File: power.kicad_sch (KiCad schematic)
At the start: 50 parts, among them J4 Conn_01x02, Q1 Q_NMOS, Q2 Q_NMOS, U2 LDL212PVR, U3 LDL212PVR, U5 LDL212PVR, U6 LDL212PVR, U8 TPS62933O, U9 LM74502

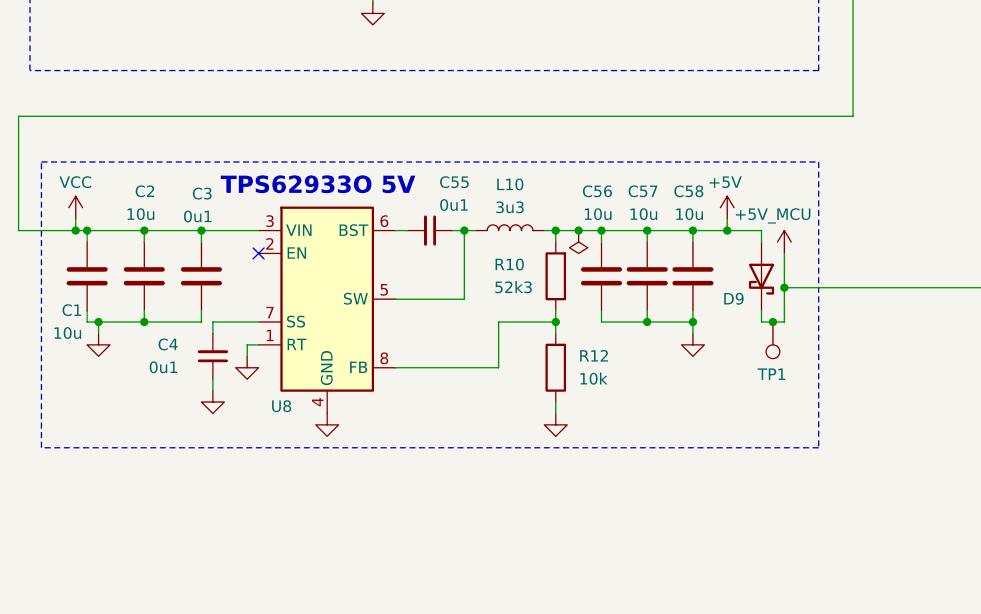
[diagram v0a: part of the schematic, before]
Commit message: schem: add buck converter PG led
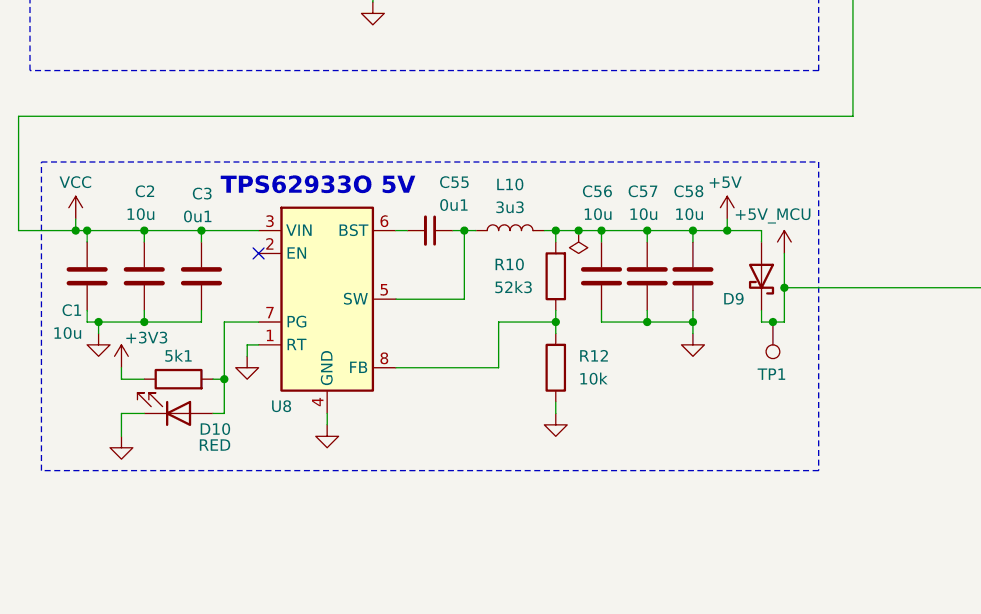
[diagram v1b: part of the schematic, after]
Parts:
- removed C4: 0u1, Capacitor_SMD:C_0402_1005Metric, symbol Device:C_Small
- added D10: RED, LED_SMD:LED_0603_1608Metric, symbol Device:LED
- added R13: 5k1, Resistor_SMD:R_0402_1005Metric, symbol Device:R
- U8: symbol Regulator_Switching:TPS62933 -> Regulator_Switching:TPS62933O
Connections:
- net +3V3: now also R13.1
- net GND: now also D10.1 (K)
- net at U8.7 (PG): now also D10.2 (A), R13.2

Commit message: schem: change red led to lower vf
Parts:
- D10: footprint LED_SMD:LED_0603_1608Metric -> LED_SMD:LED_0805_2012Metric; JLCPCB Part # C2286 -> NCD0805R1; Manufacturer Hubei KENTO Elec -> Foshan NationStar Optoelectronics; Manufacturer Part Number KT-0603R -> NCD0805R1
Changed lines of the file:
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@@
 			)
 		)
-		(property "Footprint" "LED_SMD:LED_0603_1608Metric"
+		(property "Footprint" "LED_SMD:LED_0805_2012Metric"
 			(at 69.85 130.81 0)
 			(hide yes)
@@
 			)
 		)
-		(property "JLCPCB Part #" "C2286"
+		(property "JLCPCB Part #" "NCD0805R1"
 			(at 69.85 130.81 90)
 			(hide yes)
@@
 			)
 		)
-		(property "Manufacturer" "Hubei KENTO Elec "
+		(property "Manufacturer" "Foshan NationStar Optoelectronics"
 			(at 69.85 130.81 90)
 			(hide yes)
@@
 			)
 		)
-		(property "Manufacturer Part Number" "KT-0603R"
+		(property "Manufacturer Part Number" "NCD0805R1"
 			(at 69.85 130.81 90)
 			(hide yes)

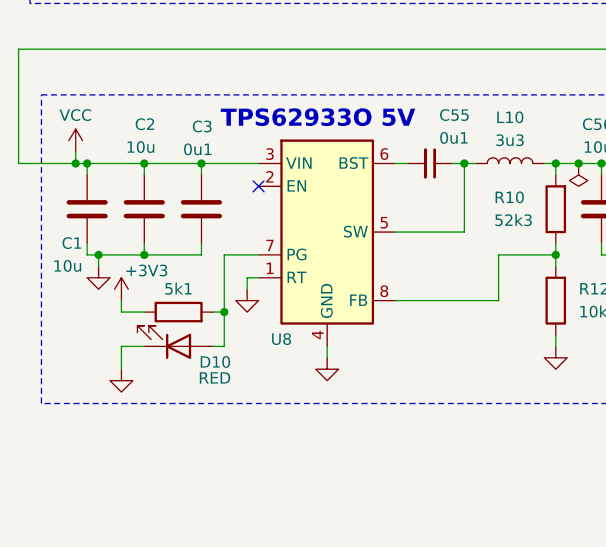
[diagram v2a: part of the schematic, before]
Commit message: schem: add PG gpio to buck converter
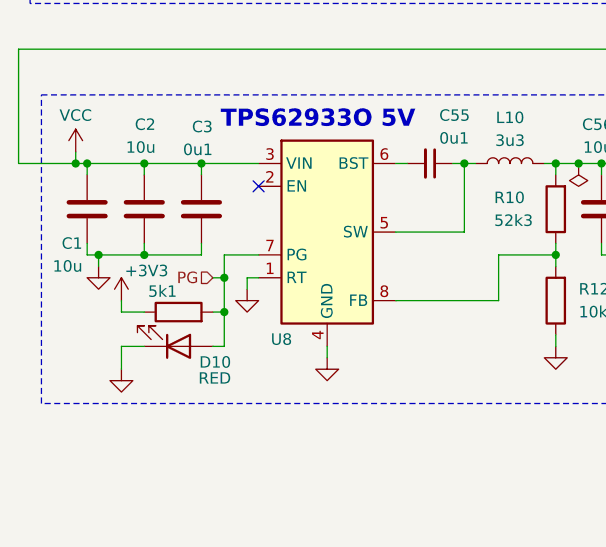
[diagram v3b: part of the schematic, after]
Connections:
- net PG: now reaches D10.2 (A), R13.2, U8.7 (PG)
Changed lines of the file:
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@@
 	)
 	(junction
+		(at 74.93 123.19)
+		(diameter 0)
+		(color 0 0 0 0)
+	)
+	(junction
 		(at 182.88 68.58)
 		(diameter 0)
@@
 	(wire
 		(pts
+			(xy 74.93 123.19) (xy 74.93 127)
+		)
+		(stroke
+			(width 0)
+			(type default)
+		)
+	)
+	(wire
+		(pts
 			(xy 205.74 102.87) (xy 205.74 100.33)
 		)
@@
 	(wire
 		(pts
-			(xy 74.93 120.65) (xy 74.93 127)
+			(xy 74.93 120.65) (xy 74.93 123.19)
 		)
 		(stroke
@@
 	(wire
 		(pts
-			(xy 78.74 120.65) (xy 74.93 120.65)
+			(xy 74.93 120.65) (xy 78.74 120.65)
 		)
 		(stroke
@@
 	(wire
 		(pts
+			(xy 73.66 123.19) (xy 74.93 123.19)
+		)
+		(stroke
+			(width 0)
+			(type default)
+		)
+	)
+	(wire
+		(pts
 			(xy 240.03 35.56) (xy 240.03 36.83)
 		)
@@
 		)
 	)
+	(hierarchical_label "PG"
+		(shape input)
+		(at 73.66 123.19 180)
+		(effects
+			(font
+				(size 1.27 1.27)
+			)
+			(justify right)
+		)
+	)
 	(symbol
 		(lib_id "power:+5V")
@@
 		)
 		(property "Value" "5k1"
-			(at 69.85 124.46 90)
+			(at 68.072 124.714 90)
 			(show_name no)
 			(do_not_autoplace no)

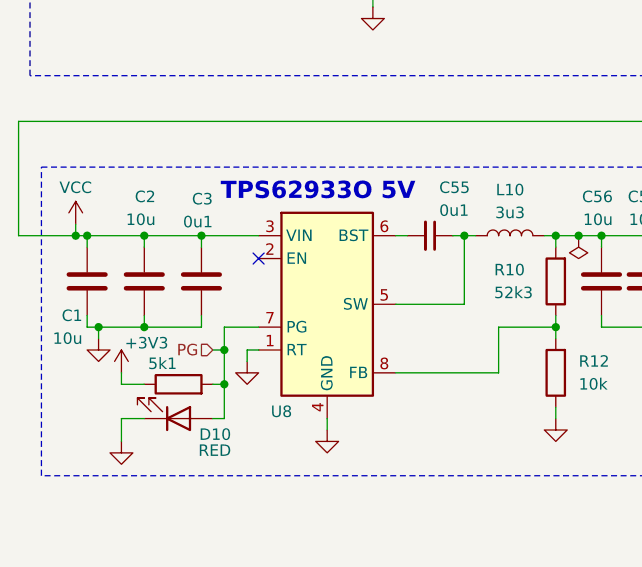
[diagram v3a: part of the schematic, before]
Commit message: schem: add buck converter disable jumper
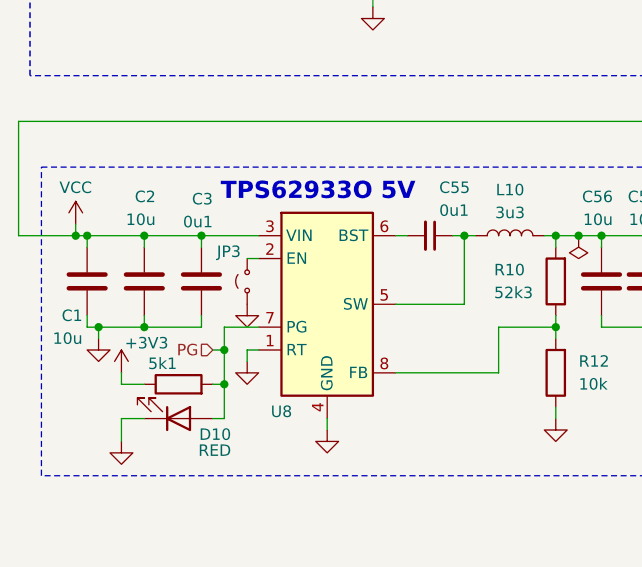
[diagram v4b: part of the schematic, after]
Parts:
- added JP3: Jumper_2_Small_Open, Connector_PinHeader_2.54mm:PinHeader_1x02_P2.54mm_Vertical, symbol Jumper:Jumper_2_Small_Open
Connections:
- net GND: now also JP3.1 (A)
- net at U8.2 (EN): now also JP3.2 (B)
- no-connect marks 1 -> 0
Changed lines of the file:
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@@
 		(color 0 0 0 0)
 	)
-	(no_connect
-		(at 78.74 113.03)
-	)
 	(wire
 		(pts
@@
 	(wire
 		(pts
+			(xy 77.47 113.03) (xy 78.74 113.03)
+		)
+		(stroke
+			(width 0)
+			(type default)
+		)
+	)
+	(wire
+		(pts
 			(xy 78.74 123.19) (xy 77.47 123.19)
 		)
@@
 	)
 	(symbol
+		(lib_id "Jumper:Jumper_2_Small_Open")
+		(at 77.47 115.57 90)
+		(unit 1)
+		(body_style 1)
+		(exclude_from_sim no)
+		(in_bom no)
+		(on_board yes)
+		(in_pos_files yes)
+		(dnp no)
+		(property "Reference" "JP3"
+			(at 75.438 112.268 90)
+			(show_name no)
+			(do_not_autoplace no)
+			(effects
+				(font
+					(size 1.27 1.27)
+				)
+			)
+		)
+		(property "Value" "Jumper_2_Small_Open"
+			(at 78.74 116.8399 90)
+			(hide yes)
+			(show_name no)
+			(do_not_autoplace no)
+			(effects
+				(font
+					(size 1.27 1.27)
+				)
+				(justify right)
+			)
+		)
+		(property "Footprint" "Connector_PinHeader_2.54mm:PinHeader_1x02_P2.54mm_Vertical"
+			(at 77.47 115.57 0)
+			(hide yes)
+			(show_name no)
+			(do_not_autoplace no)
+			(effects
+				(font
+					(size 1.27 1.27)
+				)
+			)
+		)
+		(property "Datasheet" ""
+			(at 77.47 115.57 0)
+			(hide yes)
+			(show_name no)
+			(do_not_autoplace no)
+			(effects
+				(font
+					(size 1.27 1.27)
+				)
+			)
+		)
+		(property "Description" "Jumper, 2-pole, small symbol, open"
+			(at 77.47 115.57 0)
+			(hide yes)
+			(show_name no)
+			(do_not_autoplace no)
+			(effects
+				(font
+					(size 1.27 1.27)
+				)
+			)
+		)
+		(pin "2"
+		)
+		(pin "1"
+		)
+		(instances
+			(project "s6tm-stereo-dev-1"
+				(path "/41fad0d7-0cae-453e-a16c-bdf8be036e99/16b0527c-413f-47f6-bff3-a7959715851d"
+					(reference "JP3")
+					(unit 1)
+				)
+			)
+		)
+	)
+	(symbol
 		(lib_id "power:VCC")
 		(at 137.16 48.26 0)
@@
 					(unit 1)
 				)
+			)
+		)
+	)
+	(symbol
+		(lib_id "power:GND")
+		(at 77.47 118.11 0)
+		(unit 1)
+		(body_style 1)
+		(exclude_from_sim no)
+		(in_bom yes)
+		(on_board yes)
+		(in_pos_files yes)
+		(dnp no)
+		(property "Reference" "#PWR0118"
+			(at 77.47 124.46 0)
+			(hide yes)
+			(show_name no)
+			(do_not_autoplace no)
+			(effects
+				(font
+					(size 1.27 1.27)
+				)
+			)
+		)
+		(property "Value" "GND"
+			(at 77.47 122.428 0)
+			(hide yes)
+			(show_name no)
+			(do_not_autoplace no)
+			(effects
+				(font
+					(size 1.27 1.27)
+				)
+			)
+		)
+		(property "Footprint" ""
+			(at 77.47 118.11 0)
+			(hide yes)
+			(show_name no)
+			(do_not_autoplace no)
+			(effects
+				(font
+					(size 1.27 1.27)
+				)
+			)
+		)
+		(property "Datasheet" ""
+			(at 77.47 118.11 0)
+			(hide yes)
+			(show_name no)
+			(do_not_autoplace no)
+			(effects
+				(font
+					(size 1.27 1.27)
+				)
+			)
+		)
+		(property "Description" "Power symbol creates a global label with name \"GND\" , ground"
+			(at 77.47 118.11 0)
+			(hide yes)
+			(show_name no)
+			(do_not_autoplace no)
+			(effects
+				(font
+					(size 1.27 1.27)
+				)
+			)
+		)
+		(pin "1"
+		)
+		(instances
+			(project "s6tm-stereo-dev-1"
+				(path "/41fad0d7-0cae-453e-a16c-bdf8be036e99/16b0527c-413f-47f6-bff3-a7959715851d"
+					(reference "#PWR0118")
+					(unit 1)
+				)

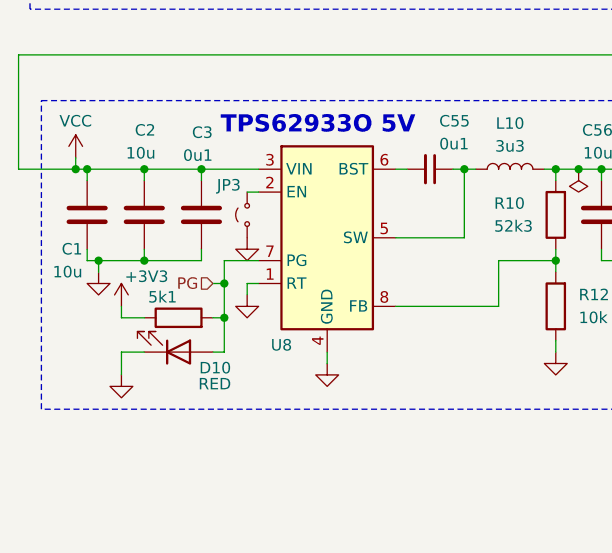
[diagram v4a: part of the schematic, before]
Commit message: schem: connect pheripherals to mcu gpios
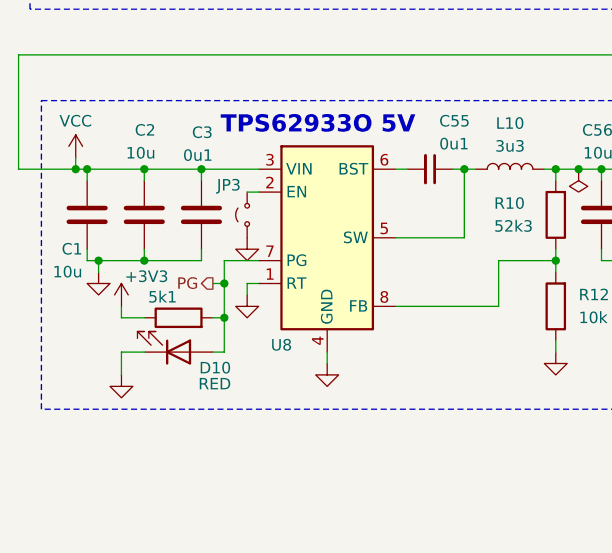
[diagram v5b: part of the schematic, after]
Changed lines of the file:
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@@
 	)
 	(hierarchical_label "PG"
-		(shape input)
+		(shape output)
 		(at 73.66 123.19 180)
 		(effects

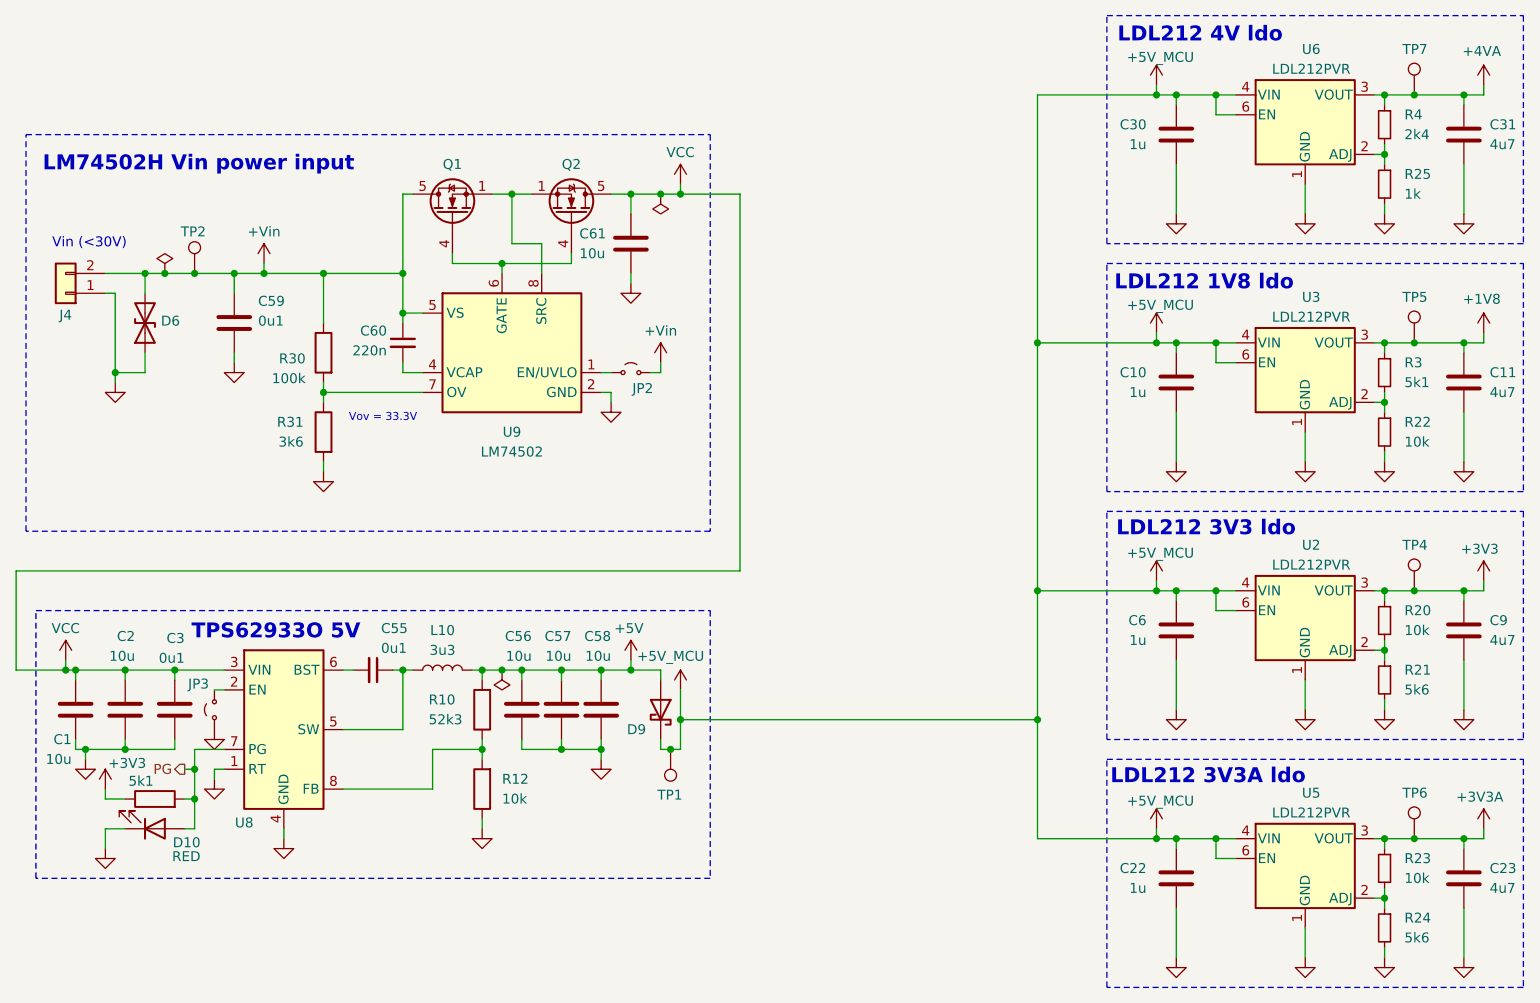
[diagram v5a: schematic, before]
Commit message: schem: add test points
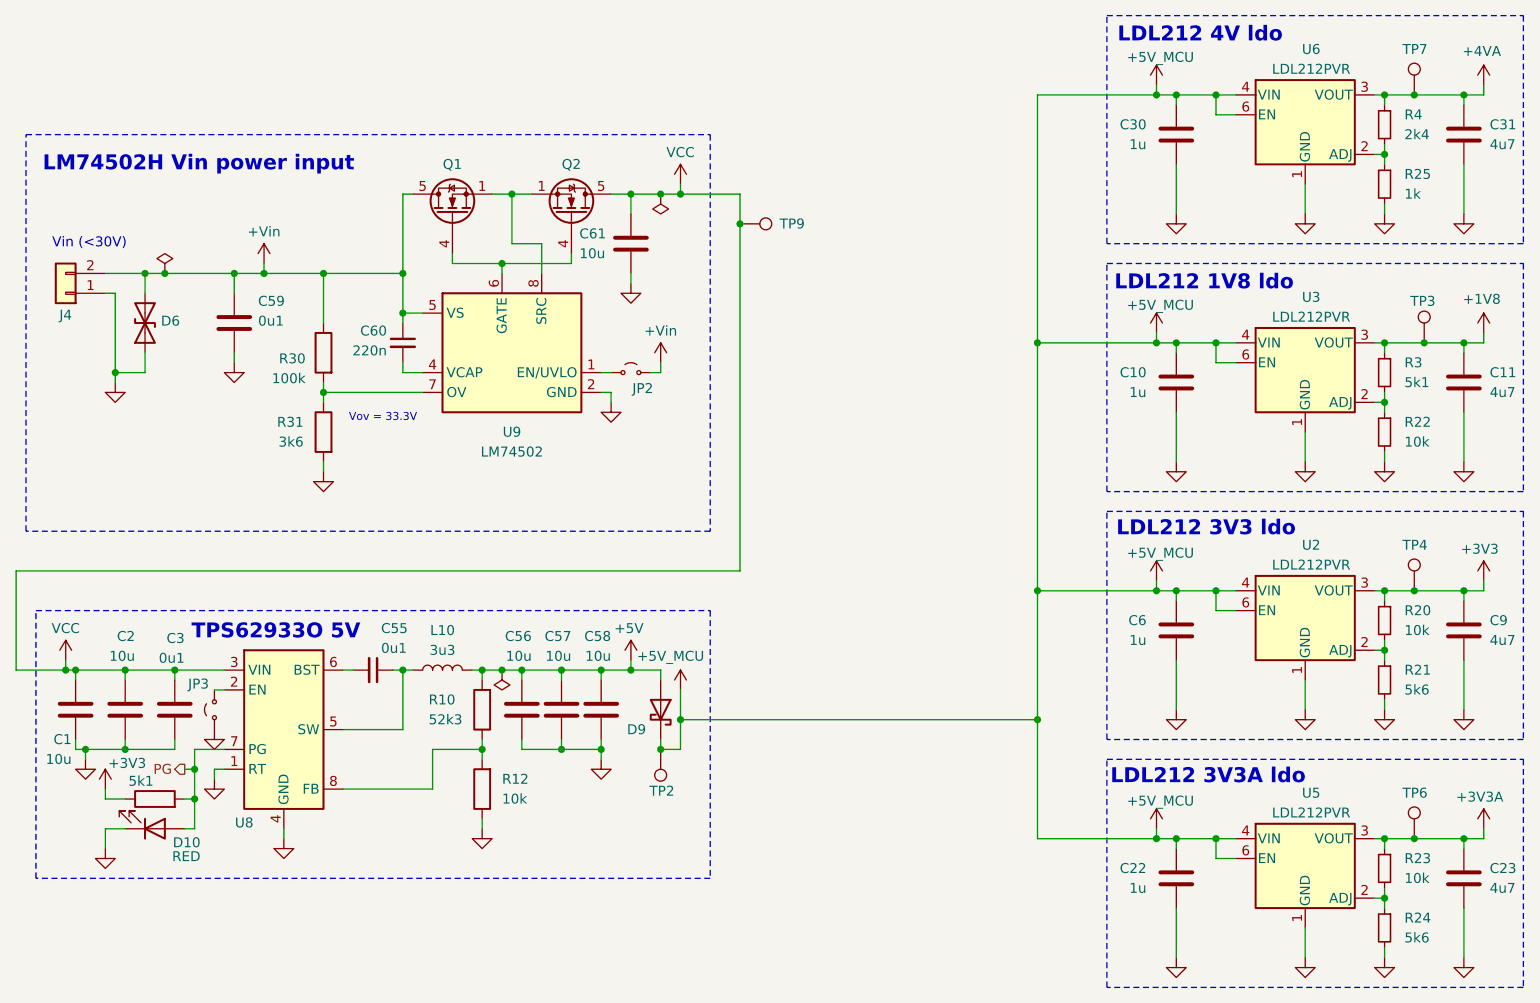
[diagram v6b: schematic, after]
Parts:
- removed TP1, TP5: TestPoint, TestPoint:TestPoint_Pad_D2.0mm, symbol Connector:TestPoint
- added TP3: TestPoint, GLCS:TestPoint_Keystone_5015_Micro_Mini, symbol Connector:TestPoint
- added TP9: TestPoint, TestPoint:TestPoint_Pad_D2.0mm, symbol Connector:TestPoint
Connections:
- net +1V8: now also TP3.1
- net +5V_MCU: now also TP2.1
- net +Vin: no longer TP2.1
- net VCC: now also TP9.1
